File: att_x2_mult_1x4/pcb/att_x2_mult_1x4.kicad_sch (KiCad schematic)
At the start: 12 parts, among them J1 AudioJack2_SwitchT, J2 AudioJack2_SwitchT, J3 AudioJack2_SwitchT, J4 AudioJack2_SwitchT, J5 AudioJack2_SwitchT, J6 AudioJack2_SwitchT, J7 AudioJack2_SwitchT, J8 AudioJack2_SwitchT

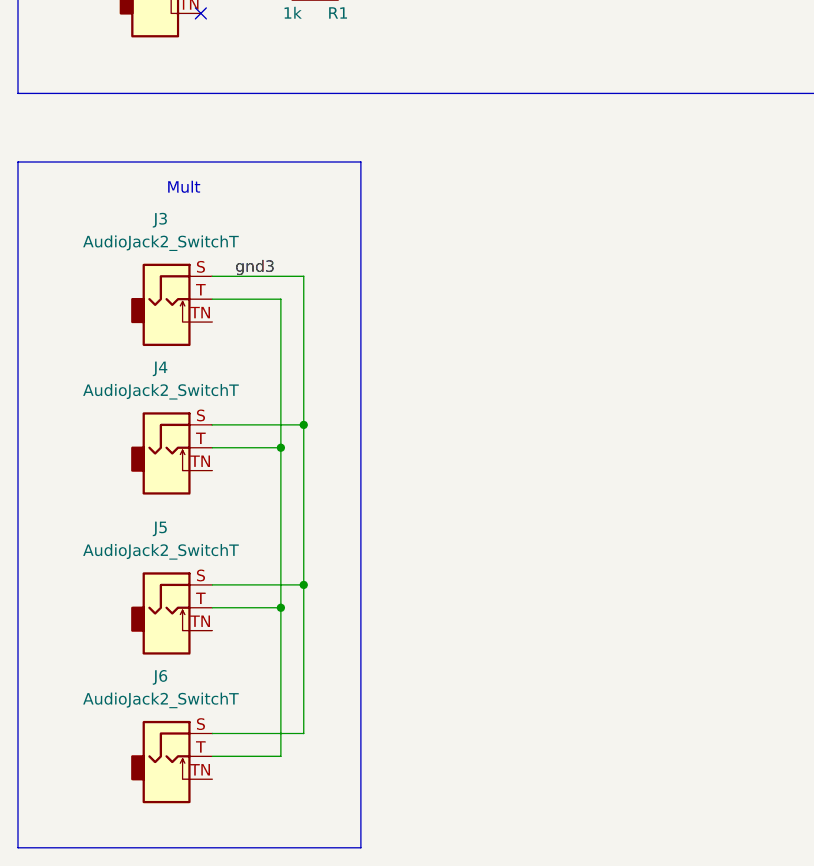
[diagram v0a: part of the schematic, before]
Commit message: extended mult to 2x3
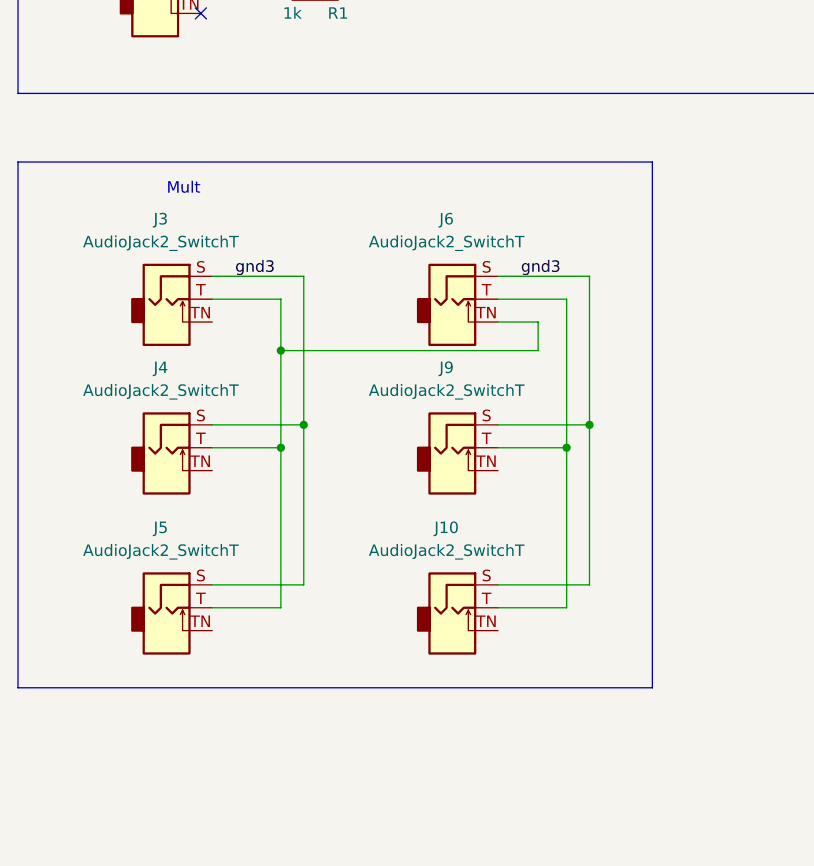
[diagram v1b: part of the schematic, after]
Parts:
- added J10, J9: AudioJack2_SwitchT, eurorack_footprints:audio_jack_pj-398sm, symbol Connector:AudioJack2_SwitchT
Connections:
- net gnd3: now also J10.S, J9.S
- net at J3.T, J4.T, J5.T: now also J6.TN; no longer J6.T
- new net: J10.T, J6.T, J9.T
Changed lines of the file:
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@@
   (junction (at 176.53 67.31) (diameter 0) (color 0 0 0 0)
   )
-  (junction (at 92.71 138.43) (diameter 0) (color 0 0 0 0)
+  (junction (at 124.46 120.65) (diameter 0) (color 0 0 0 0)
   )
   (junction (at 88.9 67.31) (diameter 0) (color 0 0 0 0)
   )
+  (junction (at 92.71 109.855) (diameter 0) (color 0 0 0 0)
+  )
   (junction (at 92.71 120.65) (diameter 0) (color 0 0 0 0)
   )
-  (junction (at 95.25 135.89) (diameter 0) (color 0 0 0 0)
+  (junction (at 127 118.11) (diameter 0) (color 0 0 0 0)
   )
   (no_connect (at 83.82 72.39))
@@
     (stroke (width 0) (type default) (color 0 0 0 0))
   )
+  (wire (pts (xy 127 135.89) (xy 116.84 135.89))
+    (stroke (width 0) (type default) (color 0 0 0 0))
+  )
+  (wire (pts (xy 116.84 104.14) (xy 124.46 104.14))
+    (stroke (width 0) (type default) (color 0 0 0 0))
+  )
+  (wire (pts (xy 92.71 109.855) (xy 121.285 109.855))
+    (stroke (width 0) (type default) (color 0 0 0 0))
+  )
   (wire (pts (xy 171.45 69.85) (xy 180.34 69.85))
     (stroke (width 0) (type default) (color 0 0 0 0))
   )
+  (wire (pts (xy 116.84 106.68) (xy 121.285 106.68))
+    (stroke (width 0) (type default) (color 0 0 0 0))
+  )
+  (wire (pts (xy 127 118.11) (xy 127 135.89))
+    (stroke (width 0) (type default) (color 0 0 0 0))
+  )
   (wire (pts (xy 199.39 69.85) (xy 199.39 62.23))
     (stroke (width 0) (type default) (color 0 0 0 0))
   )
-  (wire (pts (xy 92.71 138.43) (xy 92.71 154.94))
+  (wire (pts (xy 124.46 120.65) (xy 116.84 120.65))
+    (stroke (width 0) (type default) (color 0 0 0 0))
+  )
+  (wire (pts (xy 127 101.6) (xy 127 118.11))
+    (stroke (width 0) (type default) (color 0 0 0 0))
+  )
+  (wire (pts (xy 116.84 101.6) (xy 127 101.6))
     (stroke (width 0) (type default) (color 0 0 0 0))
   )
@@
     (stroke (width 0) (type default) (color 0 0 0 0))
   )
-  (wire (pts (xy 95.25 152.4) (xy 85.09 152.4))
-    (stroke (width 0) (type default) (color 0 0 0 0))
-  )
-  (polyline (pts (xy 63.5 88.9) (xy 101.6 88.9))
+  (polyline (pts (xy 63.5 88.9) (xy 133.985 88.9))
     (stroke (width 0) (type default) (color 0 0 0 0))
   )
@@
     (stroke (width 0) (type default) (color 0 0 0 0))
   )
-  (wire (pts (xy 92.71 154.94) (xy 85.09 154.94))
-    (stroke (width 0) (type default) (color 0 0 0 0))
-  )
-  (polyline (pts (xy 101.6 88.9) (xy 101.6 165.1))
+  (polyline (pts (xy 133.985 88.9) (xy 133.985 147.32))
+    (stroke (width 0) (type default) (color 0 0 0 0))
+  )
+  (wire (pts (xy 92.71 109.855) (xy 92.71 120.65))
+    (stroke (width 0) (type default) (color 0 0 0 0))
+  )
+  (wire (pts (xy 121.285 106.68) (xy 121.285 109.855))
     (stroke (width 0) (type default) (color 0 0 0 0))
   )
@@
     (stroke (width 0) (type default) (color 0 0 0 0))
   )
-  (wire (pts (xy 92.71 104.14) (xy 92.71 120.65))
+  (wire (pts (xy 124.46 120.65) (xy 124.46 138.43))
+    (stroke (width 0) (type default) (color 0 0 0 0))
+  )
+  (wire (pts (xy 92.71 104.14) (xy 92.71 109.855))
     (stroke (width 0) (type default) (color 0 0 0 0))
   )
@@
     (stroke (width 0) (type default) (color 0 0 0 0))
   )
+  (wire (pts (xy 127 118.11) (xy 116.84 118.11))
+    (stroke (width 0) (type default) (color 0 0 0 0))
+  )
   (wire (pts (xy 95.25 118.11) (xy 95.25 135.89))
     (stroke (width 0) (type default) (color 0 0 0 0))
   )
+  (wire (pts (xy 124.46 138.43) (xy 116.84 138.43))
+    (stroke (width 0) (type default) (color 0 0 0 0))
+  )
   (polyline (pts (xy 63.5 30.48) (xy 63.5 81.28))
     (stroke (width 0) (type default) (color 0 0 0 0))
   )
-  (polyline (pts (xy 63.5 88.9) (xy 63.5 165.1))
+  (polyline (pts (xy 63.5 88.9) (xy 63.5 147.32))
     (stroke (width 0) (type default) (color 0 0 0 0))
   )
@@
     (stroke (width 0) (type default) (color 0 0 0 0))
   )
+  (wire (pts (xy 124.46 104.14) (xy 124.46 120.65))
+    (stroke (width 0) (type default) (color 0 0 0 0))
+  )
   (polyline (pts (xy 63.5 30.48) (xy 213.36 30.48))
     (stroke (width 0) (type default) (color 0 0 0 0))
@@
     (stroke (width 0) (type default) (color 0 0 0 0))
   )
-  (wire (pts (xy 95.25 135.89) (xy 95.25 152.4))
-    (stroke (width 0) (type default) (color 0 0 0 0))
-  )
-  (polyline (pts (xy 101.6 165.1) (xy 63.5 165.1))
+  (polyline (pts (xy 133.985 147.32) (xy 63.5 147.32))
     (stroke (width 0) (type default) (color 0 0 0 0))
   )
@@
     (effects (font (size 1.27 1.27)) (justify left bottom))
   )
+  (label "gnd3" (at 119.38 101.6 0)
+    (effects (font (size 1.27 1.27)) (justify left bottom))
+  )
   (label "gnd1" (at 85.09 52.07 0)
     (effects (font (size 1.27 1.27)) (justify left bottom))
@@
   (label "gnd3" (at 87.63 101.6 0)
     (effects (font (size 1.27 1.27)) (justify left bottom))
+  )
+  (symbol (lib_id "Connector:AudioJack2_SwitchT") (at 111.76 104.14 0) (unit 1)
+    (in_bom yes) (on_board yes) (fields_autoplaced)
+    (property "Reference" "J6" (id 0) (at 111.125 95.25 0))
+    (property "Value" "AudioJack2_SwitchT" (id 1) (at 111.125 97.79 0))
+    (property "Footprint" "eurorack_footprints:audio_jack_pj-398sm" (id 2) (at 111.76 104.14 0)
+      (effects (font (size 1.27 1.27)) hide)
+    )
+    (property "Datasheet" "~" (id 3) (at 111.76 104.14 0)
+      (effects (font (size 1.27 1.27)) hide)
+    )
+    (pin "S")
+    (pin "T")
+    (pin "TN")
   )
   (symbol (lib_id "Connector:AudioJack2_SwitchT") (at 78.74 69.85 0) (unit 1)
@@
     (pin "2")
   )
-  (symbol (lib_id "Connector:AudioJack2_SwitchT") (at 80.01 154.94 0) (unit 1)
-    (in_bom yes) (on_board yes) (fields_autoplaced)
-    (property "Reference" "J6" (id 0) (at 79.375 146.05 0))
-    (property "Value" "AudioJack2_SwitchT" (id 1) (at 79.375 148.59 0))
-    (property "Footprint" "eurorack_footprints:audio_jack_pj-398sm" (id 2) (at 80.01 154.94 0)
-      (effects (font (size 1.27 1.27)) hide)
-    )
-    (property "Datasheet" "~" (id 3) (at 80.01 154.94 0)
-      (effects (font (size 1.27 1.27)) hide)
-    )
-    (pin "S")
-    (pin "T")
-    (pin "TN")
-  )
   (symbol (lib_id "Connector:AudioJack2_SwitchT") (at 80.01 104.14 0) (unit 1)
     (in_bom yes) (on_board yes) (fields_autoplaced)
@@
     (pin "TN")
   )
+  (symbol (lib_id "Connector:AudioJack2_SwitchT") (at 111.76 120.65 0) (unit 1)
+    (in_bom yes) (on_board yes) (fields_autoplaced)
+    (property "Reference" "J9" (id 0) (at 111.125 111.76 0))
+    (property "Value" "AudioJack2_SwitchT" (id 1) (at 111.125 114.3 0))
+    (property "Footprint" "eurorack_footprints:audio_jack_pj-398sm" (id 2) (at 111.76 120.65 0)
+      (effects (font (size 1.27 1.27)) hide)
+    )
+    (property "Datasheet" "~" (id 3) (at 111.76 120.65 0)
+      (effects (font (size 1.27 1.27)) hide)
+    )
+    (pin "S")
+    (pin "T")
+    (pin "TN")
+  )
   (symbol (lib_id "Device:R_Potentiometer") (at 191.77 62.23 0) (unit 1)
     (in_bom yes) (on_board yes) (fields_autoplaced)
@@
     (pin "3")
   )
+  (symbol (lib_id "Connector:AudioJack2_SwitchT") (at 111.76 138.43 0) (unit 1)
+    (in_bom yes) (on_board yes) (fields_autoplaced)
+    (property "Reference" "J10" (id 0) (at 111.125 129.54 0))
+    (property "Value" "AudioJack2_SwitchT" (id 1) (at 111.125 132.08 0))
+    (property "Footprint" "eurorack_footprints:audio_jack_pj-398sm" (id 2) (at 111.76 138.43 0)
+      (effects (font (size 1.27 1.27)) hide)
+    )
+    (property "Datasheet" "~" (id 3) (at 111.76 138.43 0)
+      (effects (font (size 1.27 1.27)) hide)
+    )
+    (pin "S")
+    (pin "T")
+    (pin "TN")
+  )
   (sheet_instances
     (path "/" (page "1"))
@@
       (reference "J5") (unit 1) (value "AudioJack2_SwitchT") (footprint "eurorack_footprints:audio_jack_pj-398sm")
     )
-    (path "/4a189efe-c023-42e2-93de-5981657b01d6"
+    (path "/12c37350-f9f4-469b-8818-063fb09c78c5"
       (reference "J6") (unit 1) (value "AudioJack2_SwitchT") (footprint "eurorack_footprints:audio_jack_pj-398sm")
     )
@@
       (reference "J8") (unit 1) (value "AudioJack2_SwitchT") (footprint "eurorack_footprints:audio_jack_pj-398sm")
     )
+    (path "/e7e135ed-da37-474a-b578-02cb1c818f87"
+      (reference "J9") (unit 1) (value "AudioJack2_SwitchT") (footprint "eurorack_footprints:audio_jack_pj-398sm")
+    )
+    (path "/fe8626f5-fc0f-40ca-9427-db1b15a52216"
+      (reference "J10") (unit 1) (value "AudioJack2_SwitchT") (footprint "eurorack_footprints:audio_jack_pj-398sm")
+    )
     (path "/1868205c-ee30-4243-a4a5-3b8be43dc87c"
